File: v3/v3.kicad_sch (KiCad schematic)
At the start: 20 parts, among them Q1 MMTB3904, Q11 MMTB3904, Q12 MMTB3904, Q2 MMTB3904, Q3 MMTB3904, Q4 MMTB3904, Q7 MMTB3904, Q8 MMTB3904

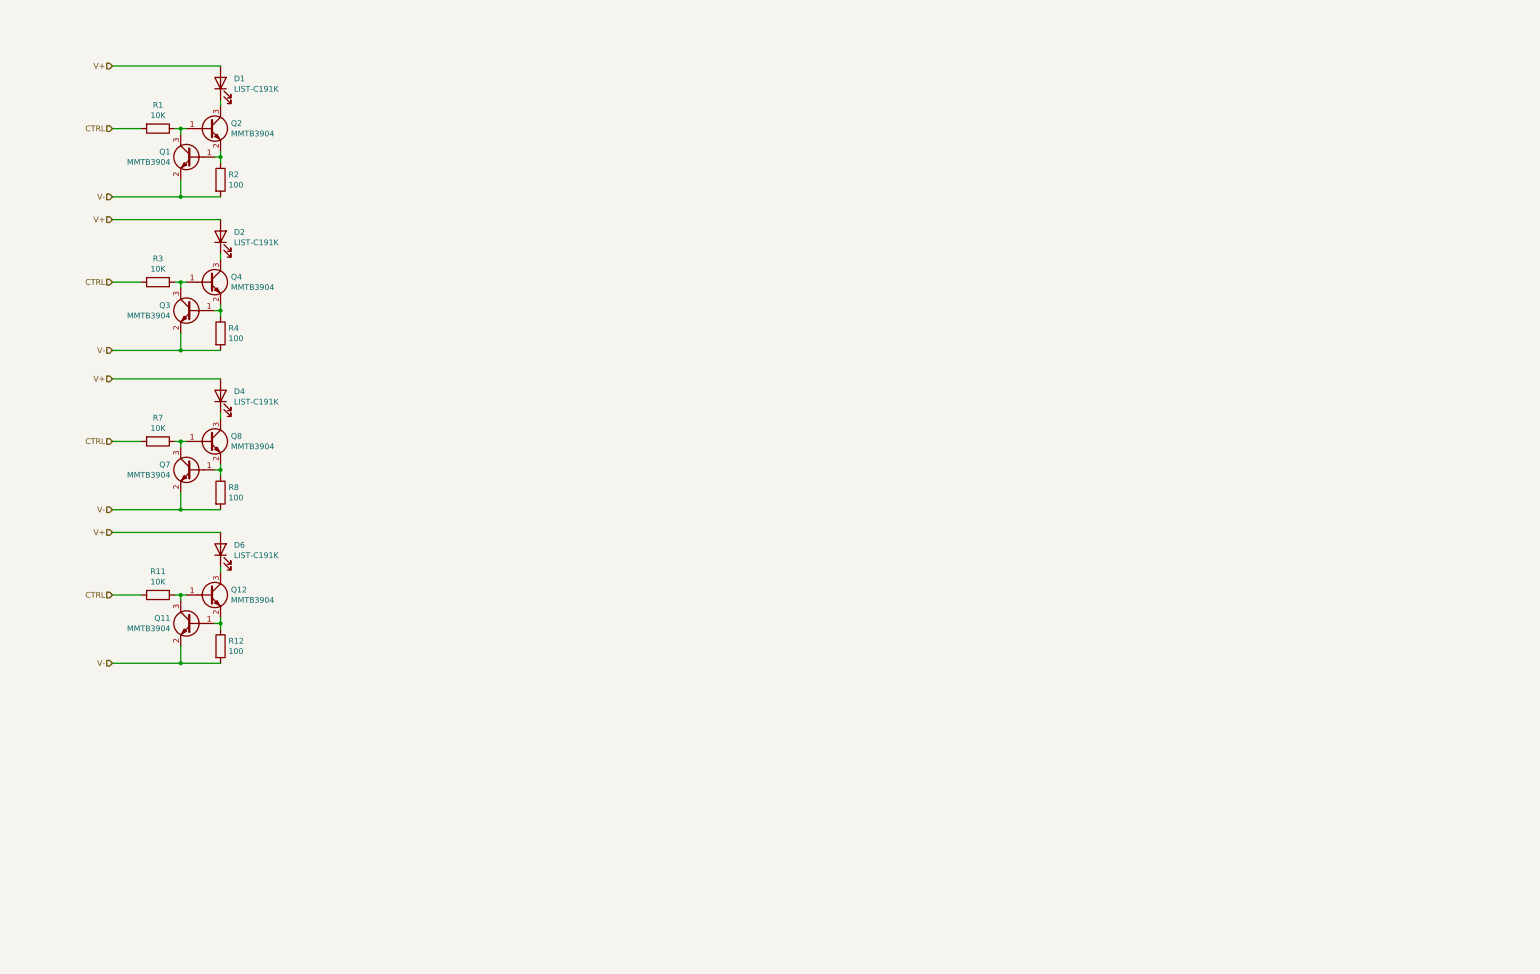
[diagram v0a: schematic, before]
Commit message: feat: design a module for red/green led
a 4 pin narrow breadboard module.
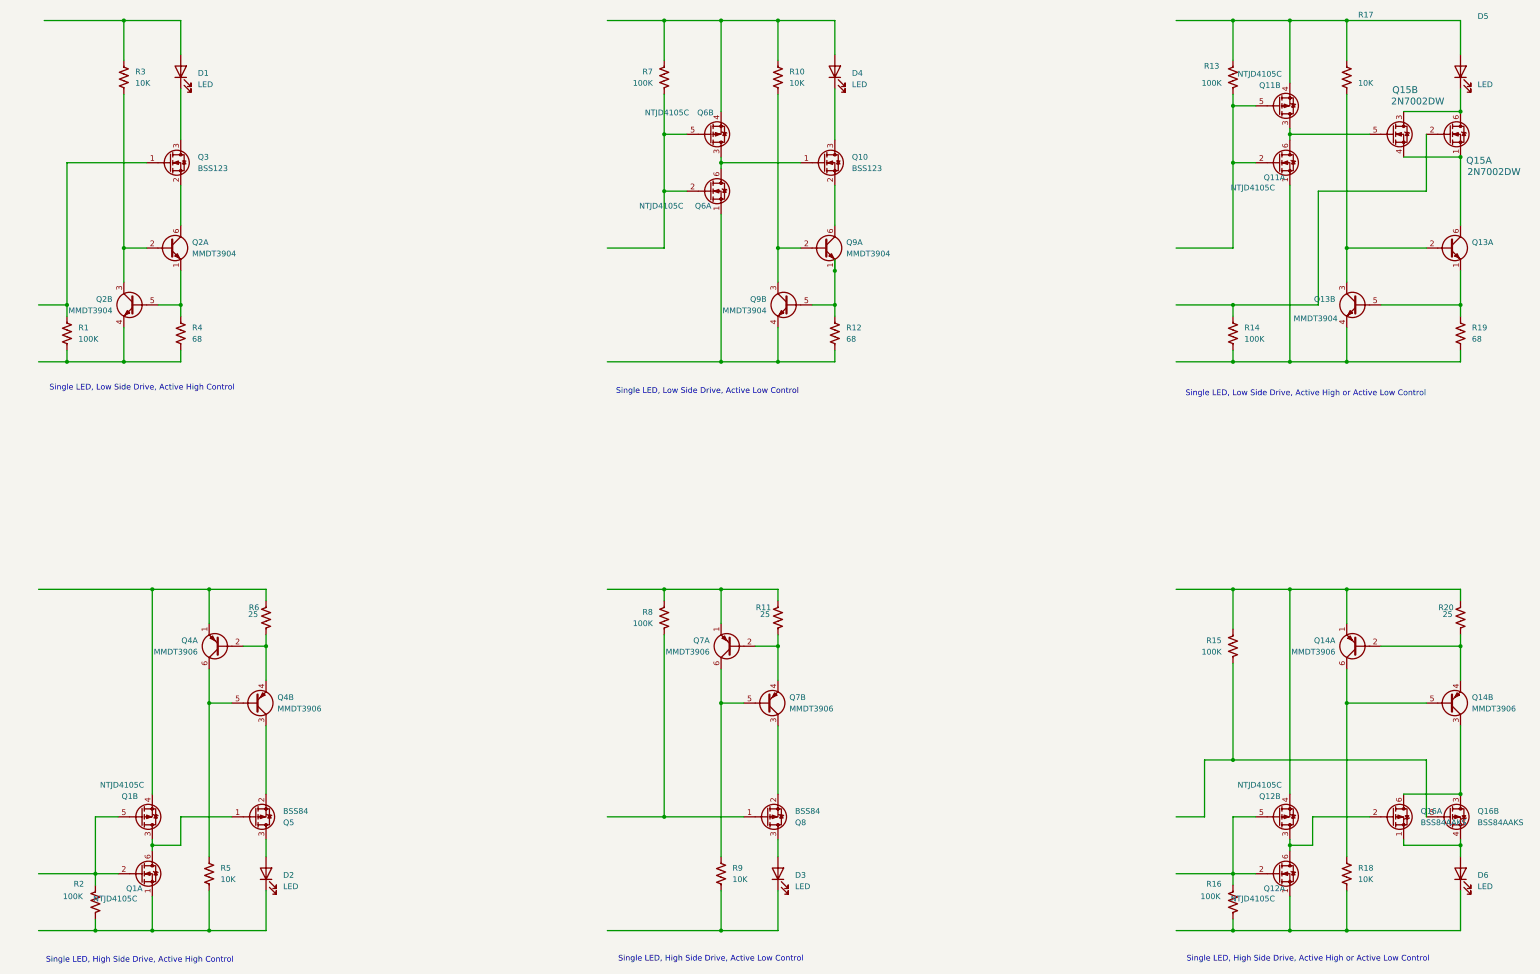
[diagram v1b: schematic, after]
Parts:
- removed Q1, Q11, Q12, Q2, Q3, Q4, Q7, Q8: MMTB3904, Package_TO_SOT_SMD:SOT-23-3, symbol Transistor_BJT:MMBT3904
- removed R1, R11, R3, R7: 10K, Resistor_SMD:R_0603_1608Metric, symbol Device:R
- removed R12, R2, R4, R8: 100, Resistor_SMD:R_0603_1608Metric, symbol Device:R
- added D3, D5: LED, LED_SMD:LED_0603_1608Metric, symbol Device:LED
- added Q1, Q11, Q12, Q6: NTJD4105C, Package_TO_SOT_SMD:SOT-363_SC-70-6, symbol symbols:NTZD3155CT1G
- added Q10, Q3: BSS123, Package_TO_SOT_SMD:SOT-23, symbol Transistor_FET:BSS123
- added Q13, Q2, Q9: MMDT3904, Package_TO_SOT_SMD:SOT-363_SC-70-6, symbol Transistor_BJT:MMDT3904
- added Q14, Q4, Q7: MMDT3906, Package_TO_SOT_SMD:SOT-363_SC-70-6, symbol Transistor_BJT:MMDT3906
- added Q15: 2N7002DW, Package_TO_SOT_SMD:SOT-363_SC-70-6, symbol symbols:2N7002DW
- added Q16: BSS84AAKS, Package_TO_SOT_SMD:SOT-363_SC-70-6, symbol 00_Local:BSS84AAKS
- added Q5, Q8: BSS84, Package_TO_SOT_SMD:SOT-23, symbol Transistor_FET:BSS84
- added R1, R13, R14, R15, R16, R2, R7, R8: 100K, Resistor_SMD:R_0603_1608Metric, symbol Device:R_US
- added R10, R17, R18, R3, R5, R9: 10K, Resistor_SMD:R_0603_1608Metric, symbol Device:R_US
- added R11, R20, R6: 25, Resistor_SMD:R_0603_1608Metric, symbol Device:R_US
- added R12, R19, R4: 68, Resistor_SMD:R_0603_1608Metric, symbol Device:R_US
- D1, D2, D4, D6: value LIST-C191K -> LED
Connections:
- net at D1.1 (K): now also Q3.3 (D)
- net at D6.1 (K): now also Q12.1 (S), R16.2, R18.2
- net at D4.1 (K): now also Q10.3 (D)
- net at D2.1 (K): now also Q1.1 (S), R2.2, R5.2
- removed net V+: D1.2 (A), D2.2 (A), D4.2 (A), D6.2 (A)
- new net: D5.1 (K), Q15.3 (D), Q15.6 (D)
- new net: D5.2 (A), Q11.4 (S), R13.1, R17.1
- new net: D4.2 (A), Q6.4 (S), R10.1, R7.1
- new net: Q9.2 (B1), Q9.3 (C2), R10.2
- new net: Q1.4 (S), Q4.1 (E1), R6.1
- new net: Q4.2 (B1), Q4.4 (E2), R6.2
- new net: Q4.5 (B2), Q4.6 (C1), R5.1
- new net: Q14.3 (C2), Q16.3 (D), Q16.6 (D)
- new net: D6.2 (A), Q16.1 (S), Q16.4 (S)
- new net: Q16.5 (G), R15.2
- new net: Q2.1 (E1), Q2.5 (B2), R4.1
- new net: Q2.2 (B1), Q2.3 (C2), R3.2
- new net: Q2.6 (C1), Q3.2 (S)
- new net: Q2.4 (E2), R1.2, R4.2
- new net: Q14.2 (B1), Q14.4 (E2), R20.2
- new net: Q14.5 (B2), Q14.6 (C1), R18.1
- new net: D1.2 (A), R3.1
- new net: Q7.1 (E1), R11.1, R8.1
- new net: Q8.1 (G), R8.2
- new net: Q7.3 (C2), Q8.2 (S)
- new net: D3.2 (A), Q8.3 (D)
- new net: Q13.6 (C1), Q15.1 (S), Q15.4 (S)
- new net: Q11.3 (D), Q11.6 (D), Q15.5 (G)
- new net: Q1.3 (D), Q1.6 (D), Q5.1 (G)
- new net: Q1.2 (G), Q1.5 (G), R2.1
- new net: Q3.1 (G), R1.1
- new net: Q11.1 (S), Q13.4 (E2), R14.2, R19.2
- new net: Q11.2 (G), Q11.5 (G), R13.2
- new net: Q13.2 (B1), Q13.3 (C2), R17.2
- new net: D3.1 (K), R9.2
- new net: Q7.2 (B1), Q7.4 (E2), R11.2
- new net: Q7.5 (B2), Q7.6 (C1), R9.1
- new net: Q15.2 (G), R14.1
- new net: Q10.1 (G), Q6.3 (D), Q6.6 (D)
- new net: Q6.2 (G), Q6.5 (G), R7.2
- new net: Q10.2 (S), Q9.6 (C1)
- new net: Q12.3 (D), Q12.6 (D), Q16.2 (G)
- new net: Q4.3 (C2), Q5.2 (S)
- new net: D2.2 (A), Q5.3 (D)
- new net: Q12.4 (S), Q14.1 (E1), R15.1, R20.1
- new net: Q12.2 (G), Q12.5 (G), R16.1
- new net: Q9.1 (E1), Q9.5 (B2), R12.1
- new net: Q6.1 (S), Q9.4 (E2), R12.2
- new net: Q13.1 (E1), Q13.5 (B2), R19.1
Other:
- note added: "Single LED, High Side Drive, Active High Control"
- note added: "Single LED, High Side Drive, Active High or Active Low Control"
- note added: "Single LED, High Side Drive, Active Low Control"
- note added: "Single LED, Low Side Drive, Active High Control"
- note added: "Single LED, Low Side Drive, Active High or Active Low Control"
- note added: "Single LED, Low Side Drive, Active Low Control"
